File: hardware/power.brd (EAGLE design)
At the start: 50 x 50 mm, 31 parts, among them IC3 LM2937, U1 LM324D, U2 LM324D

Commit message: set the distance case - PCB as defined in #2
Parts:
- moved R14 3.86 mm to (35.1, 19.3)
- moved JP2 2.00 mm to (46.5, 32.5)
- moved U$2 2.00 mm to (40.0, 14.5)
- moved R16 1.65 mm to (34.4, 9.30)
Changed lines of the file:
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@@
 <wire x1="50" y1="50" x2="0" y2="50" width="0" layer="20"/>
 <wire x1="0" y1="50" x2="0" y2="0" width="0" layer="20"/>
-<wire x1="-6" y1="-6" x2="56" y2="-6" width="0" layer="48" style="longdash"/>
-<wire x1="56" y1="-6" x2="56" y2="56" width="0" layer="48" style="longdash"/>
+<wire x1="-6" y1="-6" x2="54" y2="-6" width="0" layer="48" style="longdash"/>
+<wire x1="54" y1="-6" x2="54" y2="56" width="0" layer="48" style="longdash"/>
 <wire x1="-6" y1="-6" x2="-6" y2="56" width="0" layer="48" style="longdash"/>
-<wire x1="-6" y1="56" x2="56" y2="56" width="0" layer="48" style="longdash"/>
+<wire x1="-6" y1="56" x2="54" y2="56" width="0" layer="48" style="longdash"/>
 <text x="2.8" y="9.1" size="1.27" layer="1" font="vector" ratio="15">Power</text>
 <text x="2.2" y="6.4" size="1.016" layer="1" font="vector" ratio="15">20130116</text>
@@
 <attribute name="TP_SIGNAL_NAME" value="" x="10.16" y="45.72" size="1.778" layer="28" rot="MR0" display="off"/>
 </element>
-<element name="U$2" library="Ergaenzung" package="HOHLBUCHSE" value="HOHLBUCHSE" x="42" y="14.5"/>
-<element name="JP2" library="pinhead" package="1X04/90" value="" x="48.5" y="32.5" rot="R270"/>
+<element name="U$2" library="Ergaenzung" package="HOHLBUCHSE" value="HOHLBUCHSE" x="40" y="14.5"/>
+<element name="JP2" library="pinhead" package="1X04/90" value="" x="46.5" y="32.5" rot="R270"/>
 <element name="C1" library="rcl" package="C0805" value="10uF" x="23.8" y="20.8"/>
 <element name="U1" library="hexasense" package="SOIC127P600X175-14N" value="LM324D" x="26.8" y="36.7">
@@
 <element name="R12" library="rcl" package="R0805" value="470k" x="40" y="28.5" rot="R90"/>
 <element name="R13" library="rcl" package="R0805" value="470k" x="31.7" y="15.4" rot="R180"/>
-<element name="R14" library="rcl" package="R0805" value="470k" x="36.5" y="15.7"/>
+<element name="R14" library="rcl" package="R0805" value="470k" x="35.1" y="19.3"/>
 <element name="R15" library="rcl" package="R0805" value="47k" x="35.4" y="2.1"/>
-<element name="R16" library="rcl" package="RTRIMT93YB" value="20k" x="36" y="8.9"/>
+<element name="R16" library="rcl" package="RTRIMT93YB" value="20k" x="34.4" y="9.3"/>
 <element name="TP5" library="testpad" package="B1,27" value="TPB1,27" x="30.48" y="45.72" rot="MR0">
 <attribute name="TP_SIGNAL_NAME" value="" x="94.68" y="70.02" size="1.778" layer="28" rot="MR0" display="off"/>
@@
 <contactref element="U$1" pad="6"/>
 <contactref element="TP3" pad="TP"/>
-<wire x1="44.69" y1="33.77" x2="46.21" y2="43.91" width="0" layer="19" extent="1-1"/>
-<wire x1="44.69" y1="28.69" x2="44.69" y2="33.77" width="0" layer="19" extent="1-1"/>
-<wire x1="40" y1="24.95" x2="44.69" y2="28.69" width="0" layer="19" extent="1-1"/>
+<wire x1="42.69" y1="33.77" x2="46.21" y2="43.91" width="0" layer="19" extent="1-1"/>
+<wire x1="42.69" y1="28.69" x2="42.69" y2="33.77" width="0" layer="19" extent="1-1"/>
+<wire x1="40" y1="24.95" x2="42.69" y2="28.69" width="0" layer="19" extent="1-1"/>
 <wire x1="35.1638" y1="27.3" x2="40" y2="24.95" width="0" layer="19" extent="1-1"/>
 <wire x1="29.2638" y1="36.7" x2="35.1638" y2="27.3" width="0" layer="19" extent="1-1"/>
@@
 <wire x1="15.12" y1="36.83" x2="7.75" y2="32.745" width="0" layer="19" extent="1-1"/>
 <wire x1="15.24" y1="45.72" x2="15.12" y2="36.83" width="0" layer="19" extent="1-16"/>
-<wire x1="48.2" y1="14.5" x2="40" y2="24.95" width="0" layer="19" extent="1-1"/>
-<wire x1="37.27" y1="6.36" x2="48.2" y2="14.5" width="0" layer="19" extent="1-1"/>
+<wire x1="46.2" y1="14.5" x2="40" y2="24.95" width="0" layer="19" extent="1-1"/>
+<wire x1="35.67" y1="6.76" x2="46.2" y2="14.5" width="0" layer="19" extent="1-1"/>
 </signal>
 <signal name="+12V">
 <contactref element="IC3" pad="1"/>
 <contactref element="U$2" pad="I"/>
-<wire x1="27.88" y1="17.0512" x2="42" y2="14.5" width="0" layer="19" extent="1-1"/>
+<wire x1="27.88" y1="17.0512" x2="40" y2="14.5" width="0" layer="19" extent="1-1"/>
 </signal>
 <signal name="N$11">
@@
 <contactref element="U2" pad="3"/>
 <contactref element="JP2" pad="3"/>
-<wire x1="30.2362" y1="28.57" x2="44.69" y2="31.23" width="0" layer="19" extent="1-1"/>
+<wire x1="30.2362" y1="28.57" x2="42.69" y2="31.23" width="0" layer="19" extent="1-1"/>
 <wire x1="24.65" y1="24.4" x2="30.2362" y2="28.57" width="0" layer="19" extent="1-1"/>
 </signal>
@@
 <contactref element="R15" pad="2"/>
 <contactref element="R16" pad="3"/>
-<wire x1="36.35" y1="2.1" x2="37.27" y2="11.44" width="0" layer="19" extent="1-1"/>
+<wire x1="36.35" y1="2.1" x2="35.67" y2="11.84" width="0" layer="19" extent="1-1"/>
 </signal>
 <signal name="N$6">
 <contactref element="R16" pad="2"/>
 <contactref element="U2" pad="13"/>
-<wire x1="34.73" y1="8.9" x2="35.1638" y2="29.84" width="0" layer="19" extent="1-1"/>
+<wire x1="33.13" y1="9.3" x2="35.1638" y2="29.84" width="0" layer="19" extent="1-1"/>
 </signal>
 <signal name="N$9">
@@
 <contactref element="U2" pad="9"/>
 <contactref element="R13" pad="1"/>
-<wire x1="35.55" y1="15.7" x2="35.1638" y2="24.76" width="0" layer="19" extent="1-1"/>
-<wire x1="32.65" y1="15.4" x2="35.55" y2="15.7" width="0" layer="19" extent="1-1"/>
+<wire x1="34.15" y1="19.3" x2="35.1638" y2="24.76" width="0" layer="19" extent="1-1"/>
+<wire x1="32.65" y1="15.4" x2="34.15" y2="19.3" width="0" layer="19" extent="1-1"/>
 </signal>
 <signal name="N$14">
@@
 <contactref element="R1" pad="1"/>
 <contactref element="U1" pad="3"/>
-<wire x1="36.37" y1="40.08" x2="44.69" y2="36.31" width="0" layer="19" extent="1-1"/>
+<wire x1="36.37" y1="40.08" x2="42.69" y2="36.31" width="0" layer="19" extent="1-1"/>
 <wire x1="24.3362" y1="37.97" x2="36.37" y2="40.08" width="0" layer="19" extent="1-1"/>
 </signal>
@@
 <wire x1="35.1638" y1="28.57" x2="30.48" y2="45.72" width="0" layer="19" extent="1-16"/>
 <wire x1="35.1638" y1="23.49" x2="35.1638" y2="28.57" width="0" layer="19" extent="1-1"/>
-<wire x1="37.45" y1="15.7" x2="35.1638" y2="23.49" width="0" layer="19" extent="1-1"/>
+<wire x1="36.05" y1="19.3" x2="35.1638" y2="23.49" width="0" layer="19" extent="1-1"/>
 </signal>
 <signal name="U_M_1">

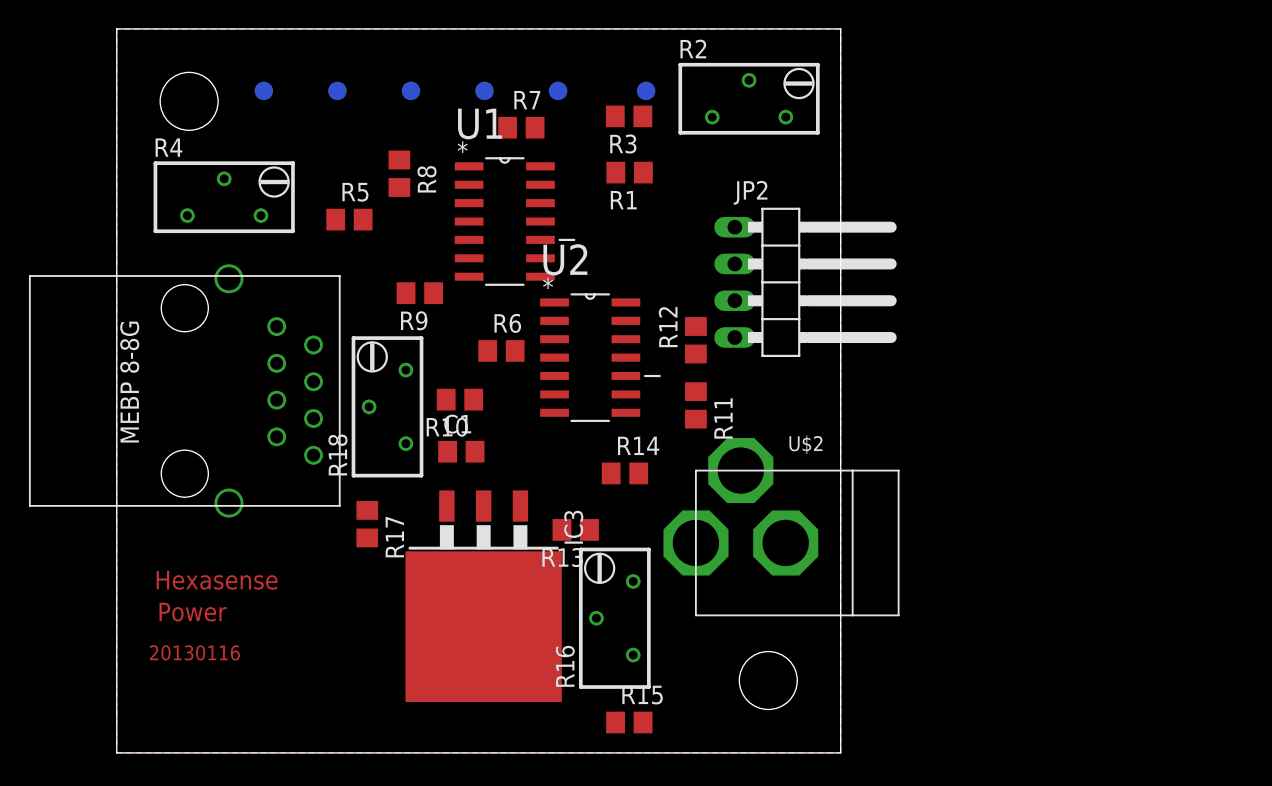
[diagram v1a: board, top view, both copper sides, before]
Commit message: preliminary placement and routing
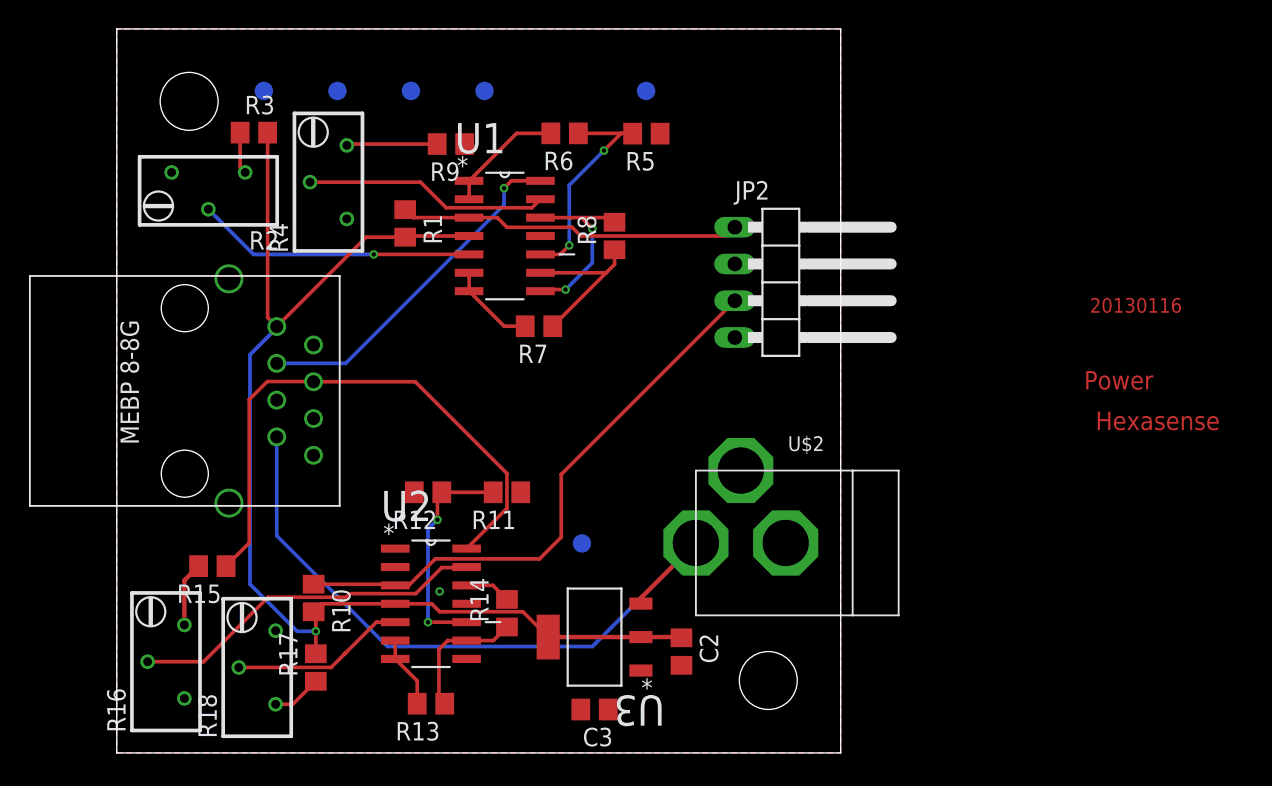
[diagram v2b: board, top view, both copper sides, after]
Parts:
- removed C1: 10uF, rcl:C0805
- removed IC3: LM2937, linear:TO263-3
- added C2, C3: 10uF, rcl:C0805
- added U3: LM1117MP-3.3, hexasense:SOT230P696X180-4N
- moved R2 37.9 mm to (6.33, 38.8), turned to 90 degrees
- moved TP5 31.3 mm to (32.1, 14.5)
- moved R16 31.1 mm to (3.40, 6.30)
- moved R15 30.8 mm to (6.60, 12.9), turned to 180 degrees
- moved R3 25.9 mm to (9.47, 42.8), turned to 0 degrees
- moved R5 21.4 mm to (36.6, 42.8), turned to 180 degrees
- moved R12 21.3 mm to (21.5, 18.0), turned to 180 degrees
- moved U2 20.2 mm to (21.7, 10.3)
- moved R18 20.1 mm to (9.70, 5.90)
- moved R10 17.0 mm to (13.6, 10.7), turned to 270 degrees
- moved R1 15.9 mm to (19.9, 36.6), turned to 270 degrees
- moved R6 15.6 mm to (30.9, 42.8), turned to 180 degrees
- moved R13 15.6 mm to (21.7, 3.40)
- moved R8 15.5 mm to (34.4, 35.7), turned to 90 degrees
- moved R11 14.4 mm to (26.9, 18.0), turned to 180 degrees
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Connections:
- removed net +12V: IC3.1, U$2.I
- new net N$15: C3.1, U3.1
- net +3V3: now also C2.1, U3.2, U3.4; no longer C1.1, IC3.3
- net +5V: now also U$2.I, U3.3
- net GND: now also C2.2, C3.2; no longer C1.2, IC3.2
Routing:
- net +3V3: track 0.00 -> 83.6 mm, vias 0 -> 1
- net +5V: track 0.00 -> 47.7 mm
- net PT100_2: track 0.00 -> 39.8 mm
- net TEMP_2: track 0.00 -> 39.5 mm
- net N$6: track 0.00 -> 24.7 mm
- net TEMP_1: track 0.00 -> 24.1 mm, vias 0 -> 1
- net PT100_1: track 0.00 -> 23.8 mm
- net OFFSET_1: track 0.00 -> 19.3 mm, vias 0 -> 1
- net N$1: track 0.00 -> 16.9 mm
- net N$9: track 0.00 -> 15.6 mm, vias 0 -> 2
- net N$2: track 0.00 -> 15.2 mm, vias 0 -> 2
- net U_M_1: track 0.00 -> 13.1 mm, vias 0 -> 2
- net OFFSET_2: track 0.00 -> 12.1 mm
- net N$8: track 0.00 -> 11.6 mm
- net N$13: track 0.00 -> 9.26 mm
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
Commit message: now passing the DRC
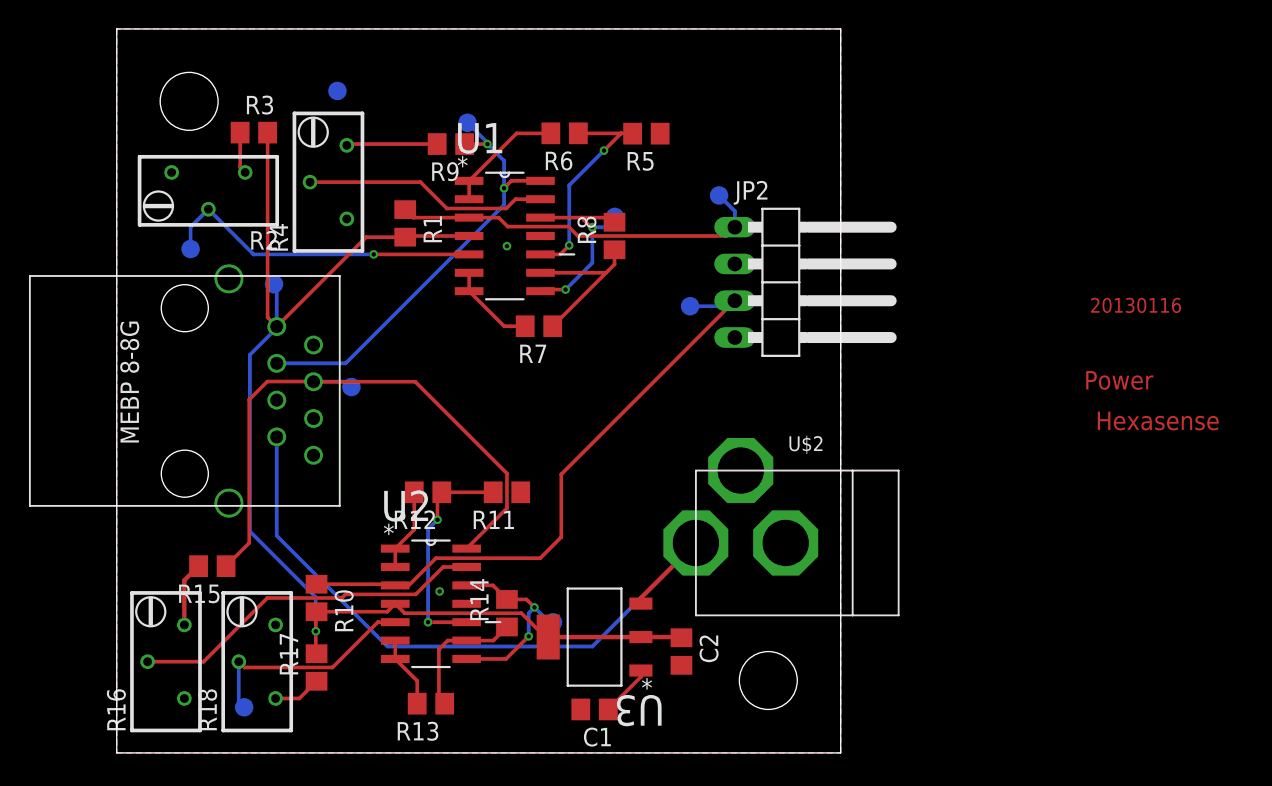
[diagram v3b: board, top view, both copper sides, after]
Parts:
- removed TP1, TP2, TP4, TP5, TP6: TPB1,27, testpad:B1,27
- added OFFSET-1, OFFSET-2, PT100-1, PT100-2, TEMP-1, TEMP-2, U_M-1, U_M-2, VCC: TPB1,27, testpad:B1,27
- moved R18 0.40 mm to (9.70, 6.30)
- moved R10 0.20 mm to (13.8, 10.7)
- moved R17 0.05 mm to (13.8, 5.90)
- renumbered C3 to C1, TP3 to GND
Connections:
- net +3V3: now also VCC.TP; no longer TP4.TP
- net OFFSET_1: now also OFFSET-1.TP
- net OFFSET_2: now also OFFSET-2.TP
- net PT100_1: now also PT100-1.TP
- net PT100_2: now also PT100-2.TP
- net TEMP_1: now also TEMP-1.TP; no longer TP2.TP
- net TEMP_2: now also TEMP-2.TP; no longer TP6.TP
- net U_M_1: now also U_M-1.TP; no longer TP1.TP
- net U_M_2: now also U_M-2.TP; no longer TP5.TP
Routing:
- net U_M_2: track 3.19 -> 14.1 mm, vias 0 -> 2
- net TEMP_1: track 24.1 -> 31.2 mm, vias 1 -> 2
- net N$10: track 0.00 -> 5.70 mm
- net N$15: track 0.00 -> 3.62 mm
- net OFFSET_2: track 12.1 -> 15.6 mm
- net OFFSET_1: track 19.3 -> 22.6 mm
- net TEMP_2: track 39.5 -> 42.2 mm
- net PT100_1: track 23.8 -> 26.4 mm
- net PT100_2: track 39.8 -> 41.9 mm
- net +3V3: track 83.6 -> 85.6 mm
- net U_M_1: track 13.1 -> 15.0 mm

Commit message: arranged position of testpads to multiples of 2.54
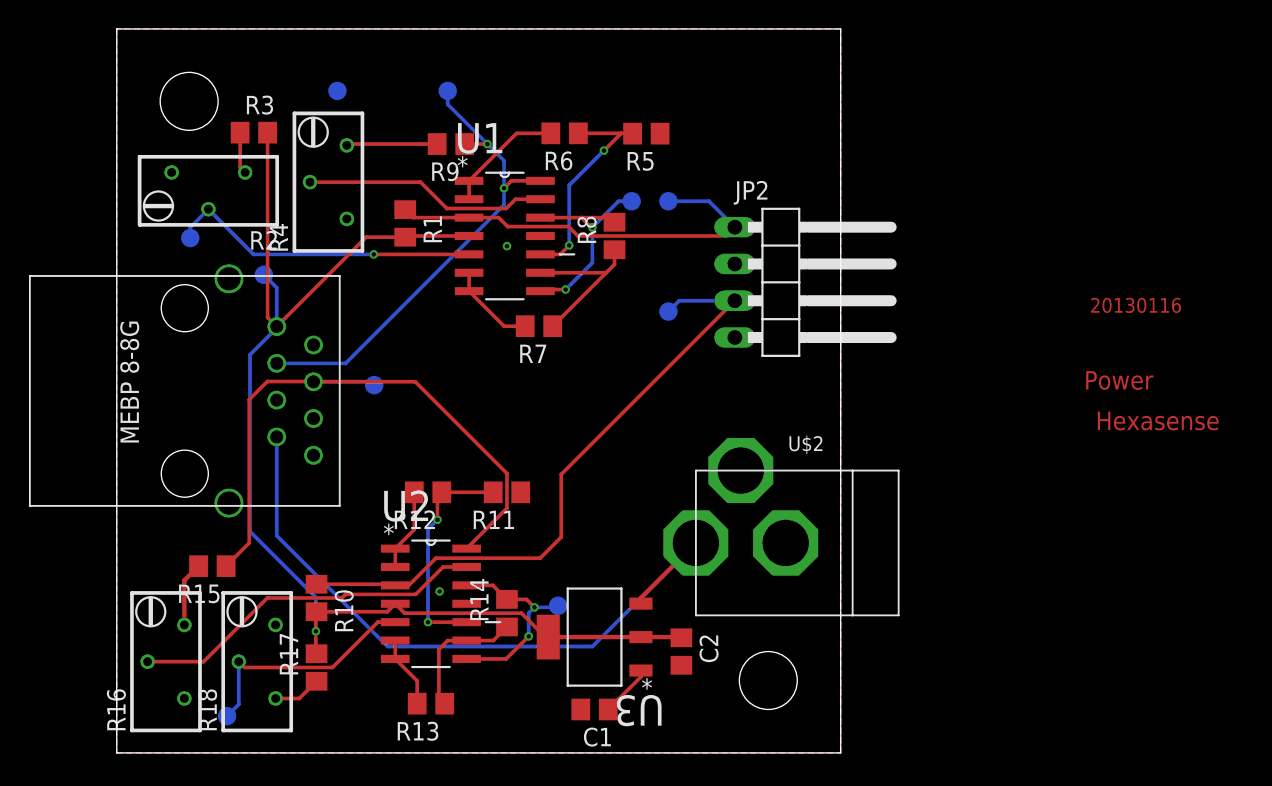
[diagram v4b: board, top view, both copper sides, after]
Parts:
- moved PT100-1 3.52 mm to (38.1, 38.1)
- moved TEMP-1 2.59 mm to (22.9, 45.7)
- moved U_M-1 1.58 mm to (35.6, 38.1)
- moved TEMP-2 1.58 mm to (17.8, 25.4)
- moved PT100-2 1.54 mm to (38.1, 30.5)
- moved OFFSET-2 1.33 mm to (7.62, 2.54)
- moved U_M-2 1.19 mm to (30.5, 10.2)
- moved VCC 0.96 mm to (10.2, 33.0)
- moved OFFSET-1 0.76 mm to (5.08, 35.6)
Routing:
- net TEMP_1: track 31.2 -> 34.1 mm
- net PT100_1: track 26.4 -> 29.1 mm
- net PT100_2: track 41.9 -> 44.1 mm
- net U_M_1: track 15.0 -> 16.6 mm
- net TEMP_2: track 42.2 -> 43.7 mm
- net +3V3: track 85.6 -> 86.5 mm
- net OFFSET_2: track 15.6 -> 16.4 mm
- net OFFSET_1: track 22.6 -> 21.8 mm
